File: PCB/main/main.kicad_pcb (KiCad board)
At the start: 2 copper layers, 19 parts, among them IC1 EL5171ISZ-T7, J1 Conn_01x33_Female, J2 Conn_01x33_Female, J3 Conn_01x33_Female, J4 Conn_01x33_Female

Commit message: updated stuff
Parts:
- removed the R3 at (83.8, 104.1)
- removed the R3 at (78.7, 96.5)
- removed the R4 at (78.6, 104.1)
- removed the R4 at (81.3, 101.6)
- added BT1: 3.7V, Battery:BatteryHolder_Keystone_1042_1x18650, F.Cu at (141.0, 96.5)
- added C10: CL10A105KB8NNNC, SamacSys_Parts:CAPC1608X90N, F.Cu at (102.5, 120.4)
- added C11: CL10A335KP8NNNC, SamacSys_Parts:CAPC1608X90N, F.Cu at (63.5, 131.8)
- added C12: CL10A335KP8NNNC, SamacSys_Parts:CAPC1608X90N, F.Cu at (60.0, 131.8)
- added C4: CL10A475KA8NQNC, SamacSys_Parts_Microcontroller:CAPC1608X95N, F.Cu at (144.7, 100.7)
- added C5: 100nF, SamacSys_Parts:CAPC1608X90N, F.Cu at (81.8, 114.6)
- added C6: CL10A475KA8NQNC, SamacSys_Parts_Microcontroller:CAPC1608X95N, F.Cu at (74.7, 113.6)
- added C7: 1uF, SamacSys_Parts:CAPC1608X90N, F.Cu at (82.9, 110.0)
- added C8: 1uF, SamacSys_Parts:CAPC1608X90N, F.Cu at (79.4, 112.3)
- added C9: CL10A105KB8NNNC, SamacSys_Parts:CAPC1608X90N, F.Cu at (98.1, 123.0)
- added D1: LED, SamacSys_Parts:LEDC1608X70N, F.Cu at (66.5, 113.9)
- added D2: BAT60J, Diode_SMD:D_SOD-323, F.Cu at (70.8, 113.9)
- added D3: BAT60J, Diode_SMD:D_SOD-323, F.Cu at (155.6, 83.1)
- added FB1: Ferrite_Bead, SamacSys_Parts:BEADC1608X95N, F.Cu at (62.0, 114.8)
- added IC2: LM358DT, SamacSys_Parts:SOIC127P600X175-8N, F.Cu at (69.9, 122.5)
- added IC3: AT24C256C-SSHL-T, SamacSys_Parts:SOIC127P600X175-8N, F.Cu at (69.9, 129.1)
- added J5: USB_B_Micro, SamacSys_Parts:MICROXNJ, F.Cu at (72.0, 105.4)
- added JP1: Jumper_3_Open, Jumper:SolderJumper-3_P1.3mm_Open_Pad1.0x1.5mm_NumberLabels, F.Cu at (57.1, 112.4)
- added MCU1: STM32F030C8Tx, Package_QFP:LQFP-48_7x7mm_P0.5mm, F.Cu at (60.0, 125.0)
- added Q1: IRF9540NPbF, SamacSys_Parts_Power:TO254P469X1042X1967-3P, F.Cu at (57.8, 108.3)
- added R10: RC0603FR-071KL, SamacSys_Parts:RESC1608X55N, F.Cu at (98.8, 120.5)
- added R11: RC0603FR-071KL, SamacSys_Parts:RESC1608X55N, F.Cu at (85.9, 129.4)
- added R12: RC0603FR-071KL, SamacSys_Parts:RESC1608X55N, F.Cu at (76.1, 120.5)
- added R13: RC0603FR-071KL, SamacSys_Parts:RESC1608X55N, F.Cu at (56.3, 131.9)
- added R3: 10k, SamacSys_Parts:RESC1608X55N, F.Cu at (84.7, 105.6)
- added R4: RC0603FR-071KL, SamacSys_Parts:RESC1608X55N, F.Cu at (89.8, 129.7)
- added R8: RC0603FR-071KL, SamacSys_Parts:RESC1608X55N, F.Cu at (90.3, 127.1)
- added R9: RC0603FR-071KL, SamacSys_Parts:RESC1608X55N, F.Cu at (94.4, 122.9)
- added U1: MCP73831-2-OT, Package_TO_SOT_SMD:SOT-23-5, F.Cu at (80.2, 106.6)
- added U2: FT232RL, Package_SO:SSOP-28_5.3x10.2mm_P0.65mm, F.Cu at (148.2, 87.7)
- added U3: MCP1700-3302E_TO92, Package_TO_SOT_THT:TO-92_Inline, F.Cu at (144.9, 97.0)
- A1, A2: footprint footprints:XDCR_ALS-PT19-315C_L177_TR8 -> SamacSys_Parts:XDCR_ALS-PT19-315C_L177_TR8
- C1: value ECQE2105KFB -> 10nF; footprint footprints:CAPRR1000W80L1850T740H2000 -> SamacSys_Parts:CAPC1608X90N
- C2: value ECQE2105KFB -> 100nF; footprint footprints:CAPRR1000W80L1850T740H2000 -> SamacSys_Parts:CAPC1608X90N
- C3: value GRM1555C1H5R1BA01D -> CL10A475KA8NQNC; footprint footprints:CAPC1005X55N -> SamacSys_Parts_Microcontroller:CAPC1608X95N
- IC1: value EL5171ISZ-T7 -> LM358DT; footprint footprints:SOIC127P600X175-8N -> SamacSys_Parts:SOIC127P600X175-8N
- R1: value AC0402FR-07536KL -> 2k; footprint footprints:RESC1005X37N -> SamacSys_Parts:RESC1005X35N
- R2: value AC0402FR-07536KL -> RC0805FR-07470RL; footprint footprints:RESC1005X37N -> SamacSys_Parts_Microcontroller:RESC2012X60N
- R5: value AC0402FR-07536KL -> RC0603FR-071KL; footprint footprints:RESC1005X37N -> SamacSys_Parts:RESC1608X55N
- R6, R7: value AC0402JR-0750RL -> AC0402FR-07536KL; footprint footprints:RESC1005X37N -> SamacSys_Parts:RESC1005X37N
- moved R7 32.5 mm to (98.1, 125.2)
- moved R5 31.5 mm to (94.4, 125.5)
- moved R6 30.9 mm to (93.9, 127.8)
- moved IC1 30.8 mm to (88.2, 122.5)
- moved A1 25.4 mm to (86.4, 127.0)
- moved C1 23.9 mm to (78.2, 114.6)
- moved R2 23.1 mm to (62.2, 112.1)
- moved A2 23.0 mm to (94.9, 120.5)
- moved C2 22.6 mm to (88.5, 105.5)
- moved R1 20.0 mm to (85.2, 112.2)
- moved C3 13.8 mm to (79.4, 110.0)
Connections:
- A1 pad 1: Vsupply -> +3v3
- A1 pad 2: Sensor Signal -> Vout1
- A2 pad 1: Vsupply -> +3v3
- A2 pad 2: Net-(A2-Pad2) -> Vout2
- C1 pad 1: GND -> Earth
- C1 pad 2: Sensor Signal -> +5V
- C2 pad 1: GND -> Earth
- C2 pad 2: Net-(A2-Pad2) -> Net-(C2-Pad2)
- C3 pad 1: Net-(C3-Pad1) -> Earth
- C3 pad 2: GND -> +5V
- IC1 pad 1: Net-(IC1-Pad1) -> Vdiff
- IC1 pad 2: Net-(A2-Pad2) -> IN1-
- IC1 pad 3: Sensor Signal -> IN1+
- IC1 pad 4: Net-(IC1-Pad4) -> -3v3
- IC1 pad 5: Net-(C3-Pad1) -> GND
- IC1 pad 6: +5v -> IN2-
- IC1 pad 7: -5v -> -3v3
- IC1 pad 8: Vdiff -> +3v3
- R1 pad 1: GND -> Net-(R1-Pad1)
- R1 pad 2: Sensor Signal -> Earth
- R2 pad 1: GND -> Net-(D1-Pad1)
- R2 pad 2: Net-(A2-Pad2) -> Net-(R2-Pad2)
- R5 pad 1: Net-(IC1-Pad1) -> GND
- R5 pad 2: Net-(IC1-Pad4) -> IN2-
- R6 pad 1: GND -> Vout1
- R6 pad 2: Net-(A2-Pad2) -> GND
- R7 pad 1: GND -> Vout2
- R7 pad 2: Sensor Signal -> GND

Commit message: git main schematics updated
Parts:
- added J5: 47346-0001, SamacSys_Parts_Power:47346-0001, F.Cu at (177.8, 96.5)
- moved Q1 115.0 mm to (170.2, 83.8)
- moved JP1 107.5 mm to (160.0, 81.3)
- moved MCU1 106.4 mm to (162.6, 96.5)
- moved J5 98.6 mm to (170.2, 96.5), turned to 90 degrees
- moved C11 90.6 mm to (140.4, 83.8)
- moved C12 88.7 mm to (134.6, 83.8)
- moved IC2 87.8 mm to (149.9, 86.4), turned to 90 degrees
- moved R13 86.9 mm to (128.7, 83.8)
- moved IC3 83.0 mm to (149.9, 106.7), turned to 90 degrees
- moved IC1 67.0 mm to (149.9, 96.5)
- moved D3 60.0 mm to (101.6, 109.2), turned to 180 degrees
- moved A1 57.6 mm to (124.5, 83.8)
- moved BT1 57.2 mm to (83.8, 99.1), turned to 90 degrees
- moved A2 56.9 mm to (142.2, 88.9)
- moved R11 56.6 mm to (119.4, 83.8)
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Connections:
- BT1 pad 2: Earth -> GND
- C1 pad 1: Earth -> GND
- C2 pad 1: Earth -> GND
- C3 pad 1: Earth -> GND
- C4 pad 1: Earth -> GND
- C5 pad 2: Earth -> GND
- C6 pad 2: Earth -> GND
- C7 pad 2: Earth -> GND
- C8 pad 2: Earth -> GND
- R1 pad 2: Earth -> GND
- R3 pad 2: Earth -> GND
- U1 pad 2: Earth -> GND
- U2 pad 18: Earth -> GND
- U2 pad 21: Earth -> GND
- U2 pad 25: Earth -> GND
- U2 pad 26: Earth -> GND
- U2 pad 7: Earth -> GND
- U3 pad 1: Earth -> GND
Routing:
- net Net-(BT1-Pad1): track 0.00 -> 208.7 mm
- net +5V: track 0.00 -> 166.7 mm
- net GND: track 0.00 -> 156.9 mm, vias 0 -> 5
- net Net-(C11-Pad2): track 0.00 -> 115.1 mm, vias 0 -> 2
- net VCC: track 0.00 -> 96.5 mm, vias 0 -> 2
- net Net-(C7-Pad1): track 0.00 -> 56.8 mm
- net /Power/D-: track 0.00 -> 39.5 mm, vias 0 -> 2
- net IN1-: track 0.00 -> 38.7 mm, vias 0 -> 2
- net Vout1: track 0.00 -> 36.5 mm, vias 0 -> 4
- net -3v3: track 0.00 -> 32.6 mm
- net Net-(R2-Pad2): track 0.00 -> 29.5 mm
- net Vout2: track 0.00 -> 26.6 mm, vias 0 -> 4
- net Vdiff: track 0.00 -> 25.6 mm, vias 0 -> 3
- net +3v3: track 0.00 -> 25.2 mm, vias 0 -> 4
- net USART1_TX: track 0.00 -> 23.9 mm, vias 0 -> 2
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- added copper zone on F.Cu, net GND
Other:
- board outline added: 121.9 x 91.4 mm

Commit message: changed made on PCD
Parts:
- moved C9 1.19 mm to (144.8, 96.5)
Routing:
- net GND: track 156.9 -> 430.3 mm, vias 5 -> 23
- net VCC: track 96.5 -> 179.8 mm, vias 2 -> 10
- net Net-(D3-Pad2): track 0.00 -> 77.3 mm, vias 0 -> 4
- net Net-(C2-Pad2): track 0.00 -> 67.9 mm, vias 0 -> 4
- net /Power/D-: track 39.5 -> 58.7 mm
- net Vout1: track 36.5 -> 47.5 mm, vias 4 -> 5
- net /PB7: track 0.00 -> 10.9 mm, vias 0 -> 2
- net /BOOT: track 0.00 -> 10.9 mm, vias 0 -> 2
- net VDD: track 0.00 -> 10.2 mm, vias 0 -> 2
- net /PF7: track 0.00 -> 10.2 mm
- net /PF6: track 0.00 -> 10.2 mm
- net /PF5: track 0.00 -> 10.2 mm
- net /PF4: track 0.00 -> 10.2 mm
- net /PF1: track 0.00 -> 10.2 mm
- net /PF0: track 0.00 -> 10.2 mm
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
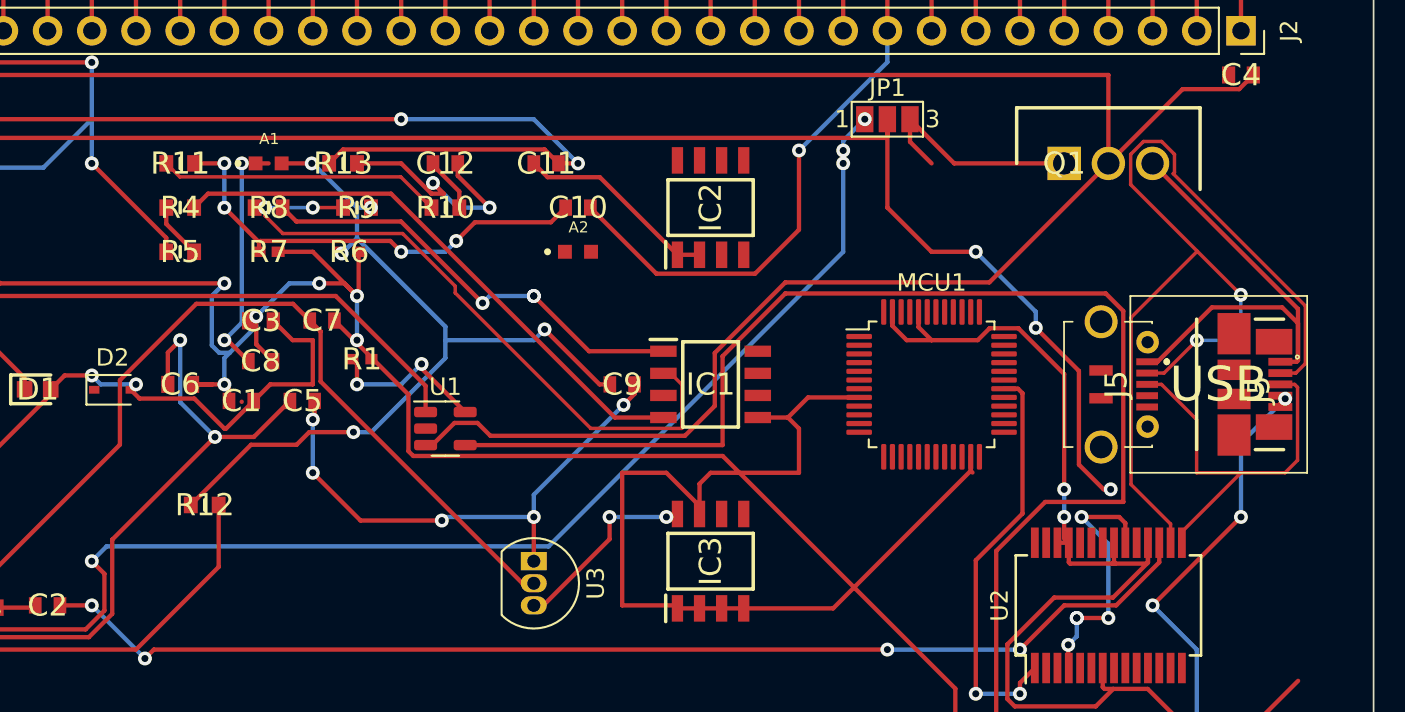
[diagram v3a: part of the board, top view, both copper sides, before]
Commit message: wired the pcb a bit
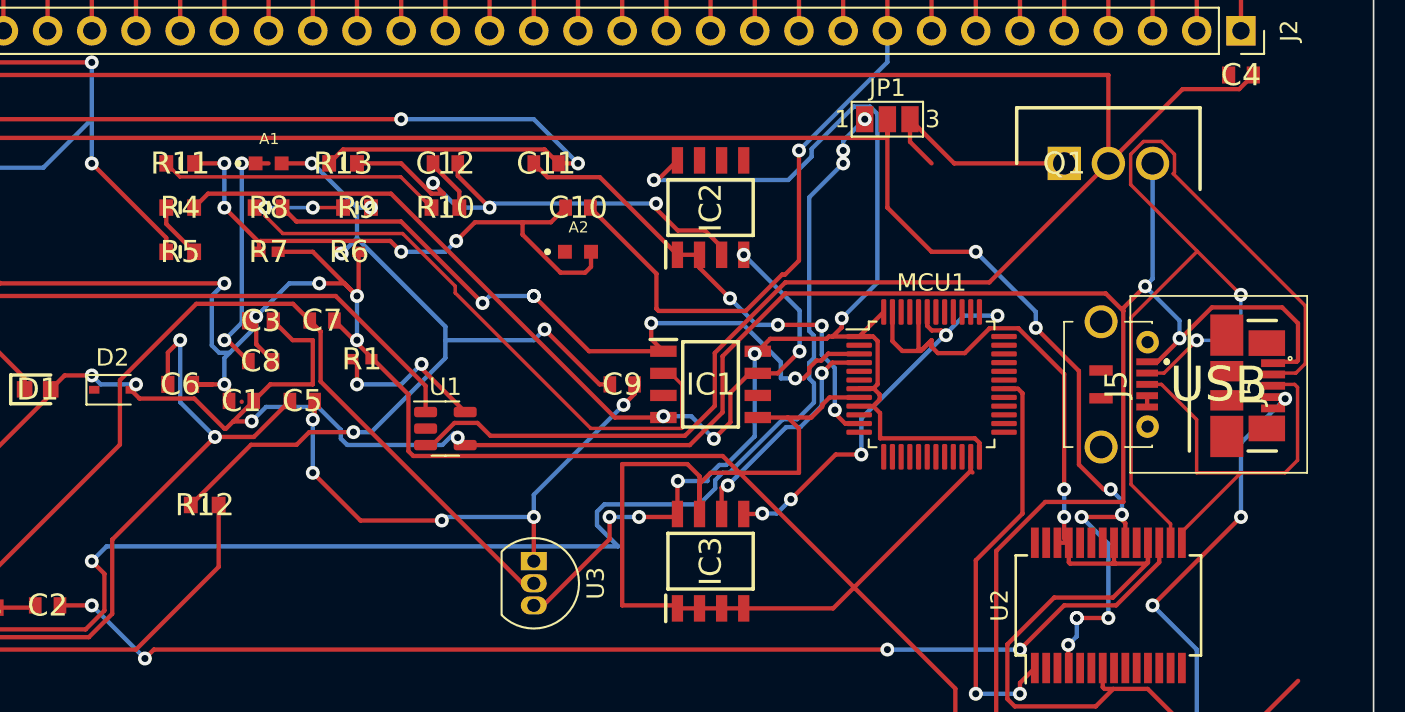
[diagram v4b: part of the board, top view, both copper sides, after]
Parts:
- moved J5 0.42 mm to (177.4, 96.6)
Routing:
- net +3v3: track 25.2 -> 92.7 mm, vias 4 -> 8
- net /microcontroller_interfacing/SDA_P43: track 0.00 -> 22.7 mm, vias 0 -> 5
- net -3v3: track 32.6 -> 51.0 mm, vias 0 -> 4
- net Vdiff: track 25.6 -> 42.1 mm, vias 3 -> 5
- net /microcontroller_interfacing/OUT1: track 11.7 -> 27.9 mm, vias 0 -> 4
- net Net-(C12-Pad2): track 13.7 -> 28.8 mm, vias 2 -> 3
- net /microcontroller_interfacing/SCL_P4: track 0.00 -> 13.8 mm, vias 0 -> 2
- net +5V: track 172.6 -> 185.1 mm, vias 2 -> 6
- net GND: track 430.3 -> 439.1 mm
- net Net-(D3-Pad2): track 77.3 -> 85.0 mm
- net Vout2: track 26.6 -> 33.2 mm
- net VCC: track 179.8 -> 181.7 mm, vias 10 -> 11
- net Earth: track 0.00 -> 0.65 mm

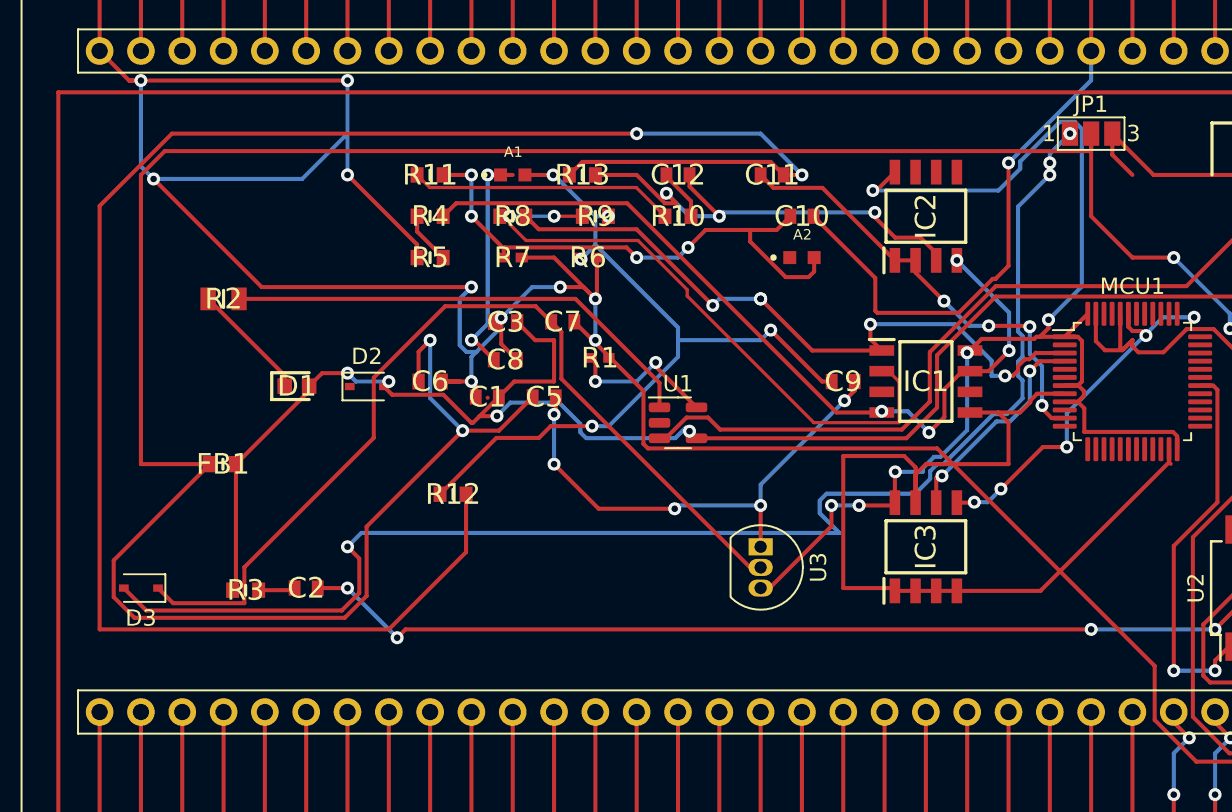
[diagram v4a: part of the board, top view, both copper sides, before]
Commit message: main with 0 DRC  errors
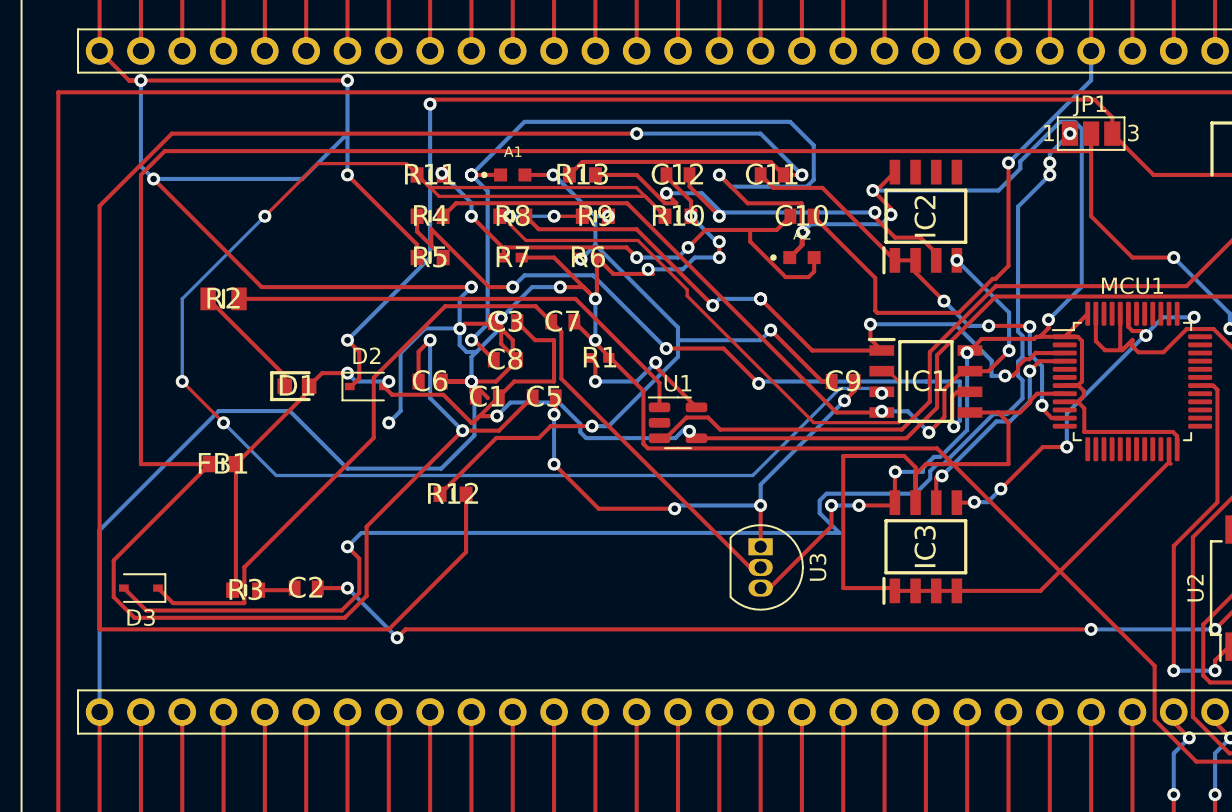
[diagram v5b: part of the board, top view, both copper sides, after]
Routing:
- net IN1+: track 16.3 -> 103.6 mm, vias 0 -> 4
- net GND: track 439.1 -> 515.8 mm, vias 23 -> 30
- net Net-(D2-Pad1): track 13.0 -> 73.5 mm, vias 0 -> 2
- net +3v3: track 92.7 -> 143.9 mm, vias 8 -> 12
- net IN2-: track 3.20 -> 48.3 mm, vias 0 -> 4
- net Vout2: track 33.2 -> 32.3 mm

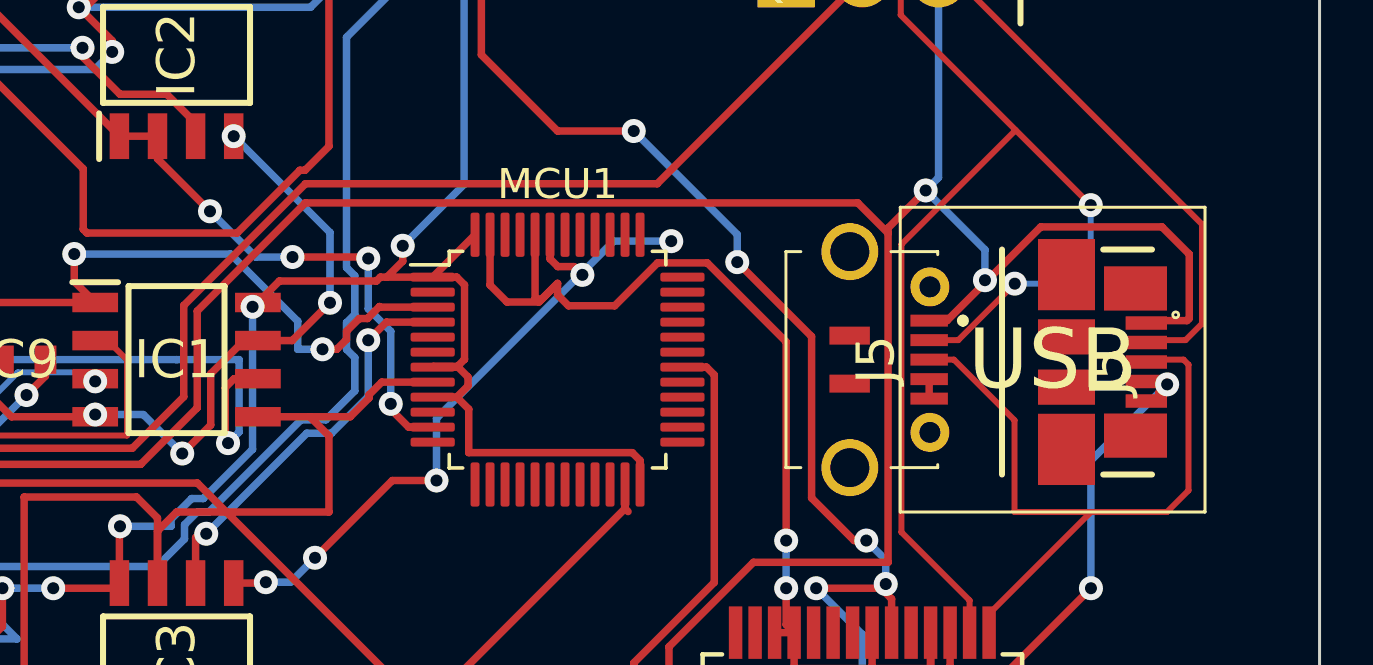
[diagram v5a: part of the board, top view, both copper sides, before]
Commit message: pcb with no errors, violations
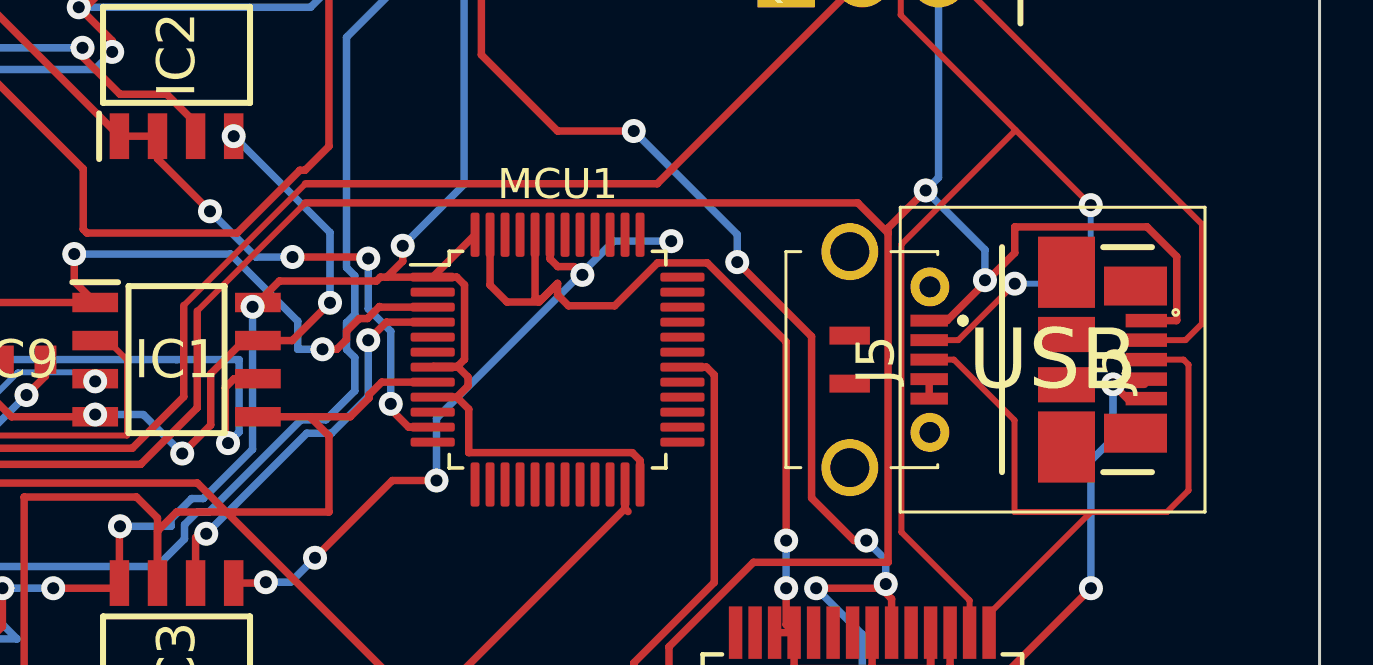
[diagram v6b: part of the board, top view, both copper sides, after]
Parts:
- moved J5 0.08 mm to (177.4, 96.5)
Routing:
- net GND: track 515.8 -> 516.8 mm
